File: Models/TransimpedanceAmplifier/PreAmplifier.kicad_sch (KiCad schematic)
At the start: 12 parts, among them J10 Conn_01x02_Pin, J9 Conn_01x02_Pin, U5 AD8615

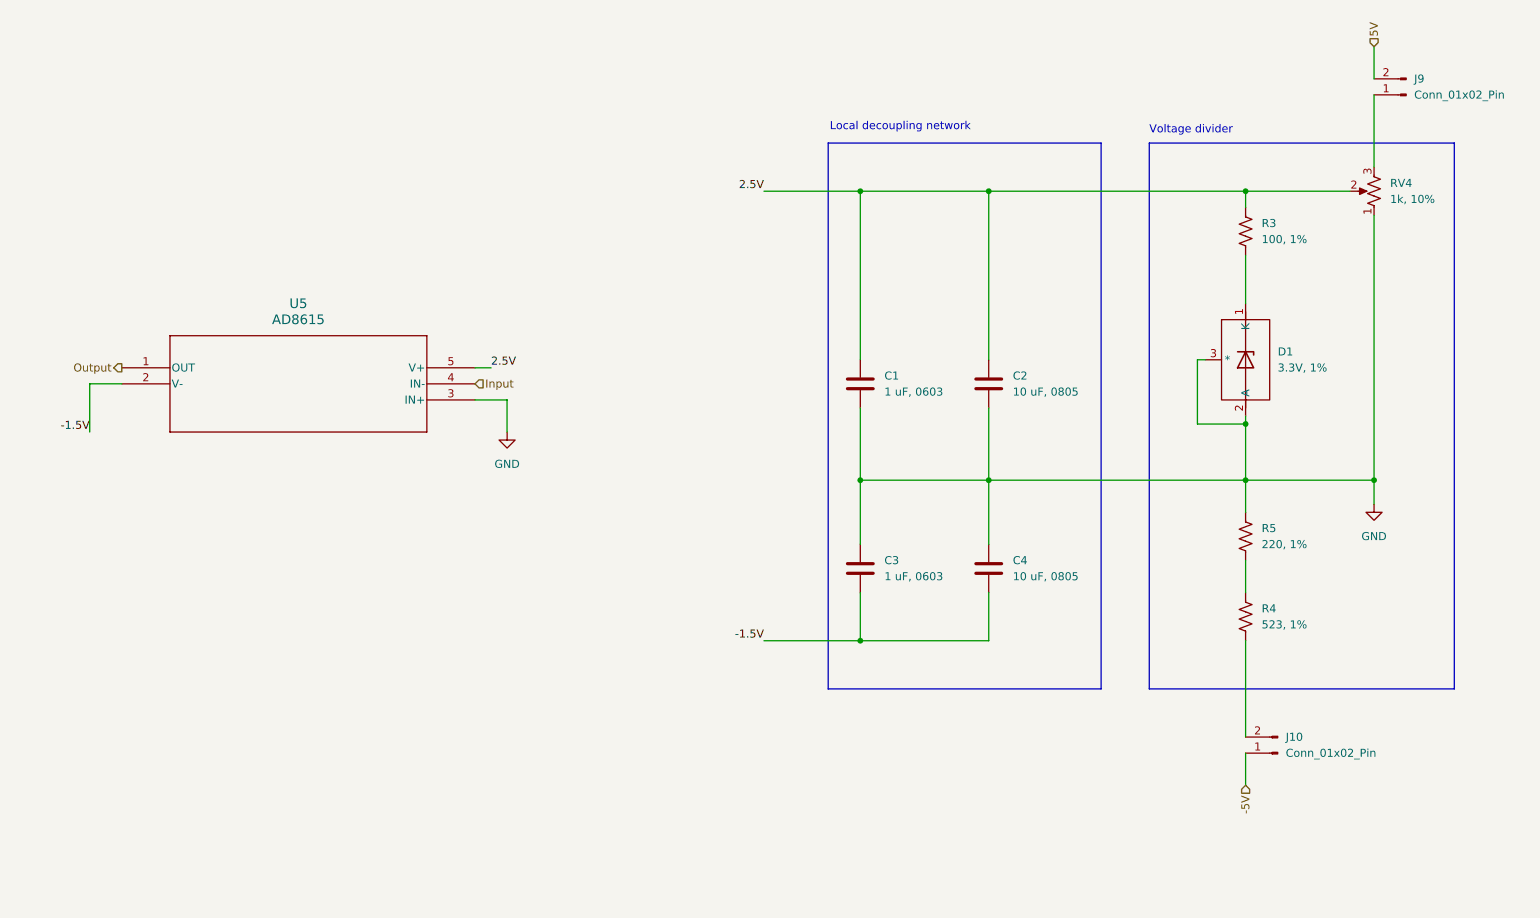
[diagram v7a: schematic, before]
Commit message: Overhauled all of the annotations
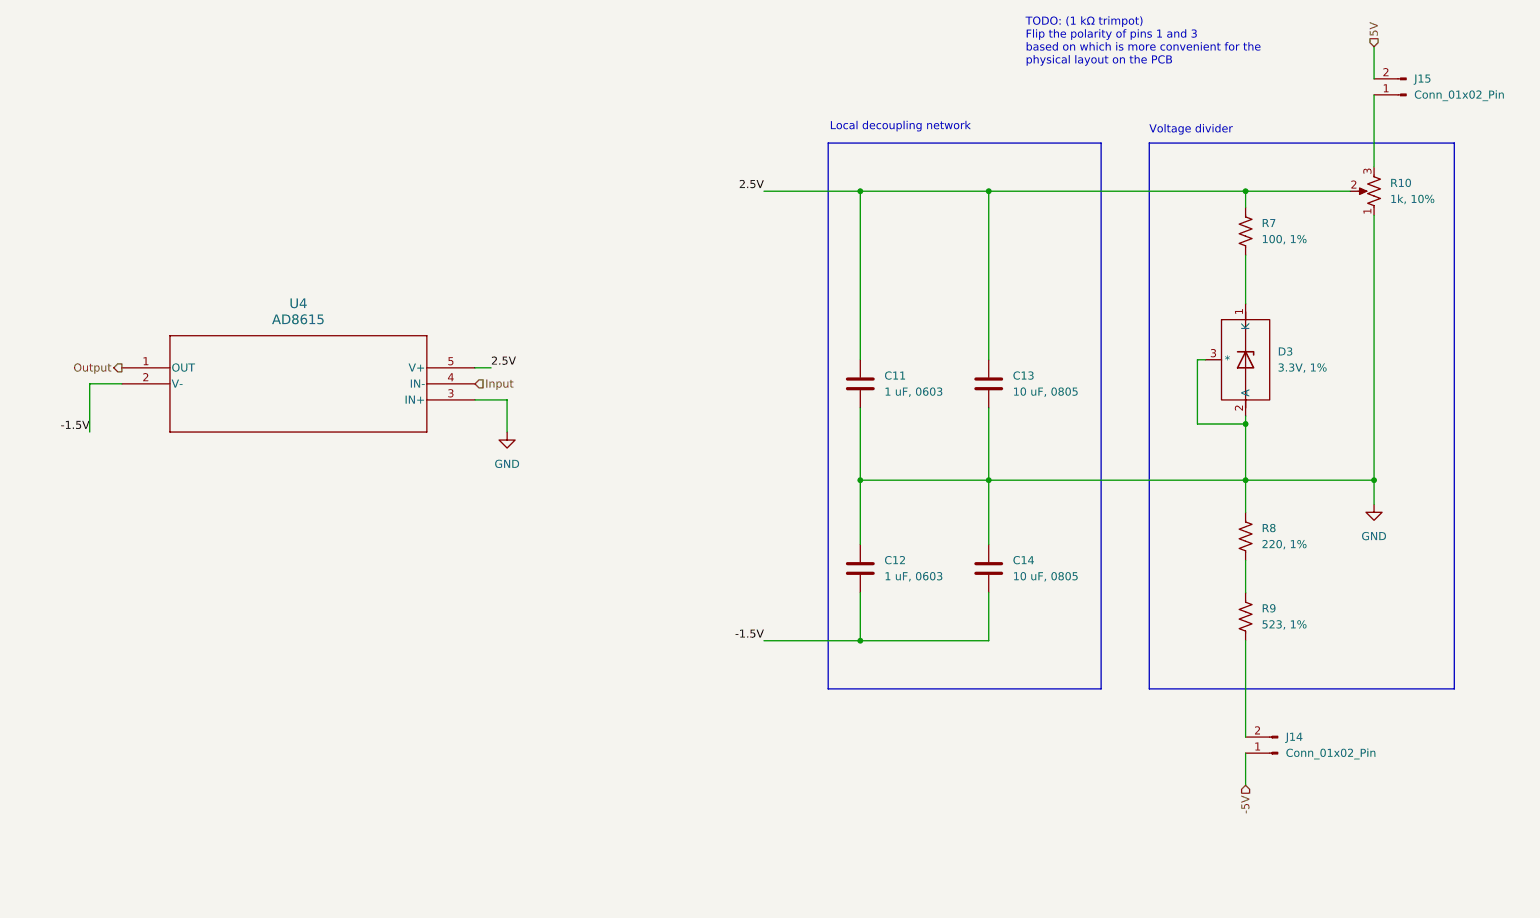
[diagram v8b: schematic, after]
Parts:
- renumbered C1 to C11, C3 to C12, C2 to C13, C4 to C14, D1 to D3, J10 to J14, J9 to J15, RV4 to R10, R3 to R7, R5 to R8, R4 to R9, U5 to U4
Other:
- note added: "TODO: (1 kΩ trimpot) Flip the polarity of pins 1 and 3 based on which is more convenient for the physical layout on the PCB"
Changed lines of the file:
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@@
+		)
+	)
+	(text "TODO: (1 kΩ trimpot)\nFlip the polarity of pins 1 and 3\nbased on which is more convenient for the\nphysical layout on the PCB"
+		(exclude_from_sim no)
+		(at 186.182 25.908 0)
+		(effects
+			(font
+				(size 1.27 1.27)
+			)
+			(justify left top)
 		)
 	)
@@
 		(dnp no)
 		(fields_autoplaced yes)
-		(property "Reference" "R3"
+		(property "Reference" "R7"
 			(at 223.52 58.4199 0)
 			(effects
@@
 			(project ""
 				(path "/ec9f2ae3-e40d-40eb-9760-2b611ee8efd1/226b3d0c-9e45-4bcf-9bef-58938aee743e/728283d1-1c30-4fdc-aa4d-bf897972ea87"
-					(reference "R3")
+					(reference "R7")
 					(unit 1)
 				)
@@
 		(dnp no)
 		(fields_autoplaced yes)
-		(property "Reference" "D1"
+		(property "Reference" "D3"
 			(at 226.06 78.7399 0)
 			(effects
@@
 			(project ""
 				(path "/ec9f2ae3-e40d-40eb-9760-2b611ee8efd1/226b3d0c-9e45-4bcf-9bef-58938aee743e/728283d1-1c30-4fdc-aa4d-bf897972ea87"
-					(reference "D1")
+					(reference "D3")
 					(unit 1)
 				)
@@
 		(on_board yes)
 		(dnp no)
-		(property "Reference" "RV4"
+		(property "Reference" "R10"
 			(at 243.84 52.0699 0)
 			(effects
@@
 			(project ""
 				(path "/ec9f2ae3-e40d-40eb-9760-2b611ee8efd1/226b3d0c-9e45-4bcf-9bef-58938aee743e/728283d1-1c30-4fdc-aa4d-bf897972ea87"
-					(reference "RV4")
+					(reference "R10")
 					(unit 1)
 				)
@@
 		(dnp no)
 		(fields_autoplaced yes)
-		(property "Reference" "R5"
+		(property "Reference" "R8"
 			(at 223.52 106.6799 0)
 			(effects
@@
 			(project ""
 				(path "/ec9f2ae3-e40d-40eb-9760-2b611ee8efd1/226b3d0c-9e45-4bcf-9bef-58938aee743e/728283d1-1c30-4fdc-aa4d-bf897972ea87"
-					(reference "R5")
+					(reference "R8")
 					(unit 1)
 				)
@@
 		(dnp no)
 		(fields_autoplaced yes)
-		(property "Reference" "C1"
+		(property "Reference" "C11"
 			(at 163.83 82.5499 0)
 			(effects
@@
 			(project ""
 				(path "/ec9f2ae3-e40d-40eb-9760-2b611ee8efd1/226b3d0c-9e45-4bcf-9bef-58938aee743e/728283d1-1c30-4fdc-aa4d-bf897972ea87"
-					(reference "C1")
+					(reference "C11")
 					(unit 1)
 				)
@@
 		(dnp no)
 		(fields_autoplaced yes)
-		(property "Reference" "C3"
+		(property "Reference" "C12"
 			(at 163.83 111.7599 0)
 			(effects
@@
 			(project "TransimpedanceAmplifier"
 				(path "/ec9f2ae3-e40d-40eb-9760-2b611ee8efd1/226b3d0c-9e45-4bcf-9bef-58938aee743e/728283d1-1c30-4fdc-aa4d-bf897972ea87"
-					(reference "C3")
+					(reference "C12")
 					(unit 1)
 				)
@@
 		(dnp no)
 		(fields_autoplaced yes)
-		(property "Reference" "#PWR01"
+		(property "Reference" "#PWR017"
 			(at 241.3 109.22 0)
 			(effects
@@
 			(project ""
 				(path "/ec9f2ae3-e40d-40eb-9760-2b611ee8efd1/226b3d0c-9e45-4bcf-9bef-58938aee743e/728283d1-1c30-4fdc-aa4d-bf897972ea87"
-					(reference "#PWR01")
+					(reference "#PWR017")
 					(unit 1)
 				)
@@
 		(dnp no)
 		(fields_autoplaced yes)
-		(property "Reference" "#PWR05"
+		(property "Reference" "#PWR016"
 			(at 104.14 97.79 0)
 			(effects
@@
 			(project ""
 				(path "/ec9f2ae3-e40d-40eb-9760-2b611ee8efd1/226b3d0c-9e45-4bcf-9bef-58938aee743e/728283d1-1c30-4fdc-aa4d-bf897972ea87"
-					(reference "#PWR05")
+					(reference "#PWR016")
 					(unit 1)
 				)
@@
 		(dnp no)
 		(fields_autoplaced yes)
-		(property "Reference" "C2"
+		(property "Reference" "C13"
 			(at 184.15 82.5499 0)
 			(effects
@@
 			(project ""
 				(path "/ec9f2ae3-e40d-40eb-9760-2b611ee8efd1/226b3d0c-9e45-4bcf-9bef-58938aee743e/728283d1-1c30-4fdc-aa4d-bf897972ea87"
-					(reference "C2")
+					(reference "C13")
 					(unit 1)
 				)
@@
 		(dnp no)
 		(fields_autoplaced yes)
-		(property "Reference" "J9"
+		(property "Reference" "J15"
 			(at 247.65 35.5599 0)
 			(effects
@@
 			(project ""
 				(path "/ec9f2ae3-e40d-40eb-9760-2b611ee8efd1/226b3d0c-9e45-4bcf-9bef-58938aee743e/728283d1-1c30-4fdc-aa4d-bf897972ea87"
-					(reference "J9")
+					(reference "J15")
 					(unit 1)
 				)
@@
 		(dnp no)
 		(fields_autoplaced yes)
-		(property "Reference" "R4"
+		(property "Reference" "R9"
 			(at 223.52 119.3799 0)
 			(effects
@@
 			(project ""
 				(path "/ec9f2ae3-e40d-40eb-9760-2b611ee8efd1/226b3d0c-9e45-4bcf-9bef-58938aee743e/728283d1-1c30-4fdc-aa4d-bf897972ea87"
-					(reference "R4")
+					(reference "R9")
 					(unit 1)
 				)
@@
 		(dnp no)
 		(fields_autoplaced yes)
-		(property "Reference" "J10"
+		(property "Reference" "J14"
 			(at 227.33 139.6999 0)
 			(effects
@@
 			(project "TransimpedanceAmplifier"
 				(path "/ec9f2ae3-e40d-40eb-9760-2b611ee8efd1/226b3d0c-9e45-4bcf-9bef-58938aee743e/728283d1-1c30-4fdc-aa4d-bf897972ea87"
-					(reference "J10")
+					(reference "J14")
 					(unit 1)
 				)
@@
 		(dnp no)
 		(fields_autoplaced yes)
-		(property "Reference" "C4"
+		(property "Reference" "C14"
 			(at 184.15 111.7599 0)
 			(effects
@@
 			(project "TransimpedanceAmplifier"
 				(path "/ec9f2ae3-e40d-40eb-9760-2b611ee8efd1/226b3d0c-9e45-4bcf-9bef-58938aee743e/728283d1-1c30-4fdc-aa4d-bf897972ea87"
-					(reference "C4")
+					(reference "C14")
 					(unit 1)
 				)
@@
 		(dnp no)
 		(fields_autoplaced yes)
-		(property "Reference" "U5"
+		(property "Reference" "U4"
 			(at 71.12 71.12 0)
 			(effects
@@
 			(project ""
 				(path "/ec9f2ae3-e40d-40eb-9760-2b611ee8efd1/226b3d0c-9e45-4bcf-9bef-58938aee743e/728283d1-1c30-4fdc-aa4d-bf897972ea87"
-					(reference "U5")
+					(reference "U4")
 					(unit 1)
 				)
